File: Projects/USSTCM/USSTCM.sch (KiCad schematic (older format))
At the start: 26 parts, among them IC1 REG1117, IC2 REG1117, Q1 DMG1012T, Q2 DMG1012T, U1 RASPI

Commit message: sync for working with liz
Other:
- moved on the sheet: ACT55, C1, C10, C15, C17, C18, C19, C2, C20, C46, C6, C8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

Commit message: Refactoring Compute Module project for 2017 USST KiCad library format
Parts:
- ACT55, PWR1: symbol LED_LEDCHIP-LED0603 -> LED
- C1, C10, C17, C18, C19, C2, C20, C46, C9: symbol RCL_C-EUC0805 -> C
- C15: symbol RCL_C-EUC0603 -> C
- C6, C8: symbol RCL_CPOL-EU153CLV-0605 -> CP
- IC1, IC2: symbol BURR-BROWN_REG1117 -> REG1117
- Q1, Q2: symbol TRANSISTOR-FET_BSA223SP -> Q_PMOS_GDS
- R1, R2, R21, R3, R35, R4, R5: symbol RCL_R-EU_R0603 -> R
- U1: symbol RASPI_RASPI -> RASPI_CM
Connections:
- net 1V8: now also C6.1, R2.1; no longer C6.+, R2.2
- net 3V3: now also C8.1, R21.1, R35.1; no longer C8.+, R21.2, R35.2
- net GND: now also C6.2, C8.2, PWR1.1 (K), Q2.2 (D), R1.2, R3.1, R4.1, R5.1; no longer C6.-, C8.-, PWR1.C, Q2.3 (S), R1.1, R3.2, R4.2, R5.2
- net GPIO28: now also R4.2; no longer R4.1
- net GPIO29: now also R3.2; no longer R3.1
- net GPIO44: now also R5.2; no longer R5.1
- net VUSB_BOOT: now also R1.1; no longer R1.2
- removed net N$1: PWR1.A, R21.1
- net N$3: no longer names the net of Q1.2 (D)
- net N$3: now also ACT55.1 (K), Q2.3 (S); no longer U1.2 (EMMC_DISABLE_N)
- removed net N$4: ACT55.A, R35.1
- removed net N$5: ACT55.C, Q1.3 (S), Q2.2 (D)
- net N$6: no longer names the net of Q2.1 (G), U1.90 (GPIO47_1V8)
- net N$6: now also R2.2; no longer R2.1
- new net: ACT55.2 (A), R35.2
- new net: Q1.3 (S), U1.2 (EMMC_DISABLE_N)
- new net: PWR1.2 (A), R21.2
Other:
- moved on the sheet: IC1, IC2, U1

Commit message: More organization of CMIO board
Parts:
- removed C1, C17, C18, C19, C2, C20, C46: 10u, USSTCM:RCL_C0805, symbol C
- removed C6, C8: ~, USSTCM:RCL_153CLV-0605, symbol CP
- removed IC1, IC2: REG1117, USSTCM:BURR-BROWN_SOT223, symbol REG1117
- removed PWR1: ~, USSTCM:LED_CHIP-LED0603, symbol LED
- removed R21: 1k8, USSTCM:RCL_R0603, symbol R
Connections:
- net 1V8 renamed +1V8
- net 3V3 renamed +3V3
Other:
- note added: "DAC 2v5 is Unused"
- note added: "NOTE: Default Device Tree Source\nhttps://github.com/raspberrypi/firmware/blob/master/extra/dt-blob.dts"
- note added: "This block works with the USB interface to diable the EMMC for flashing"

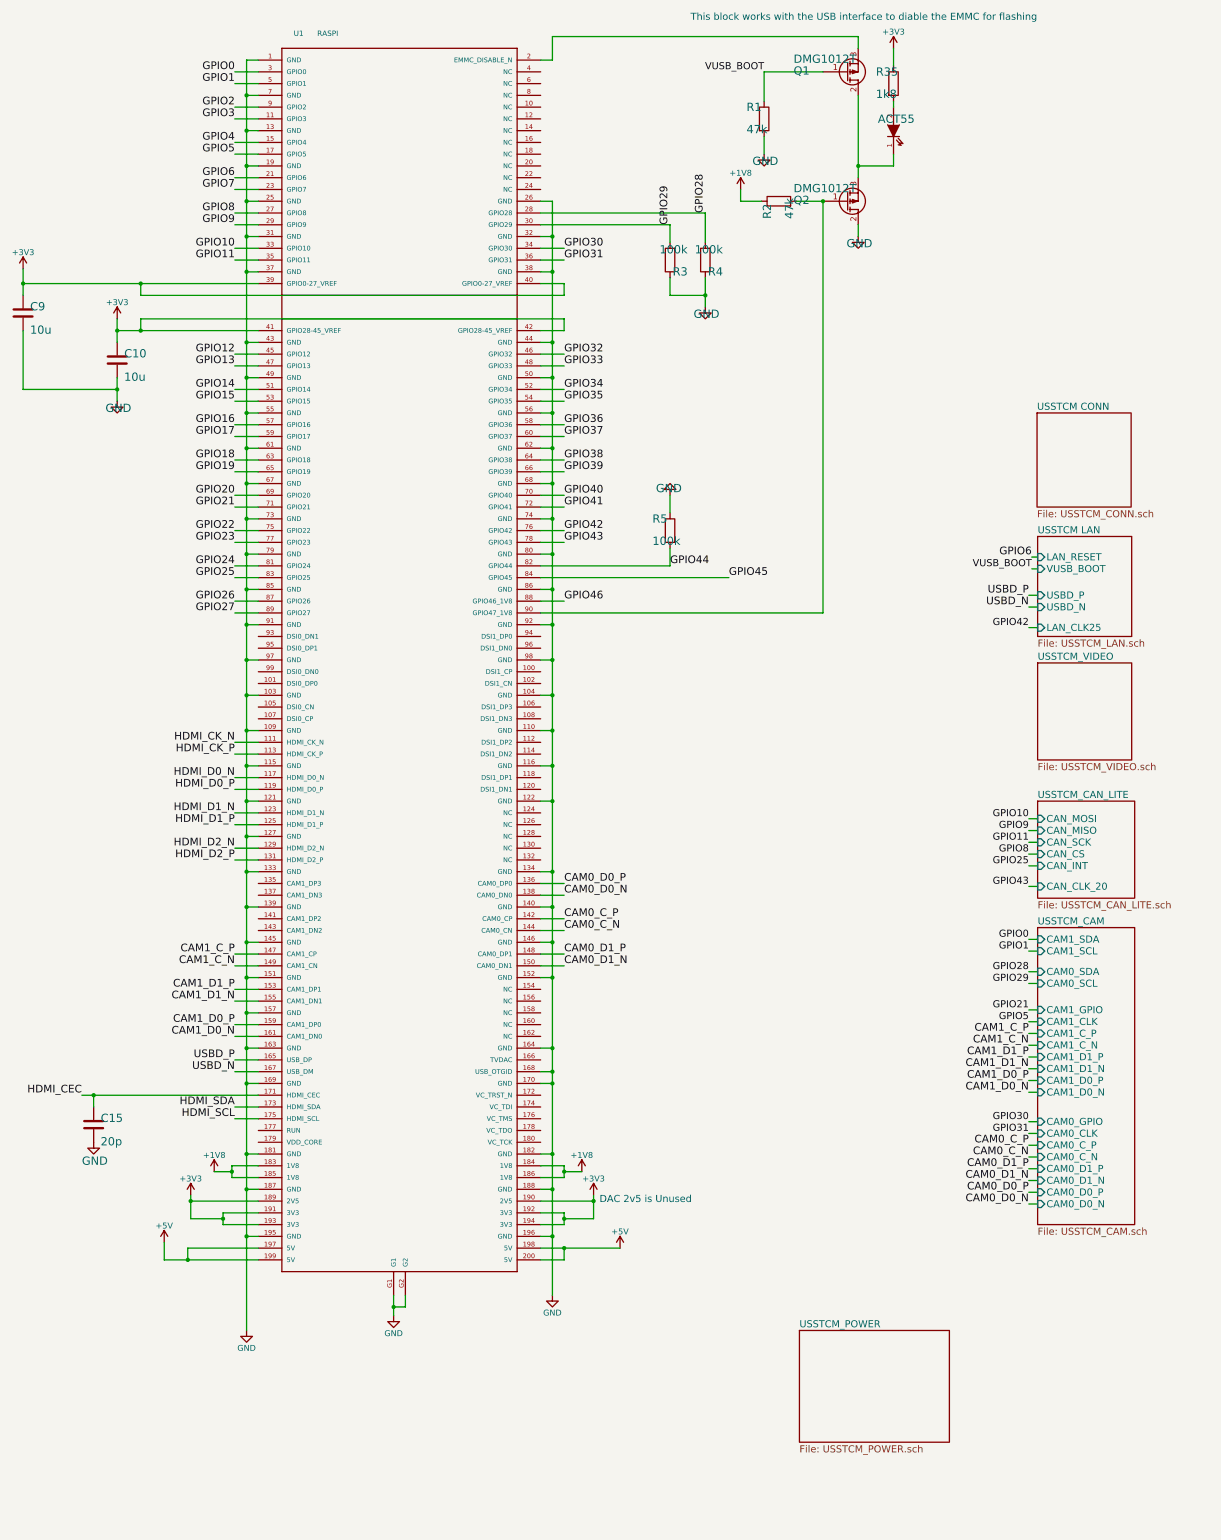
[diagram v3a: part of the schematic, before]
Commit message: added differential routes
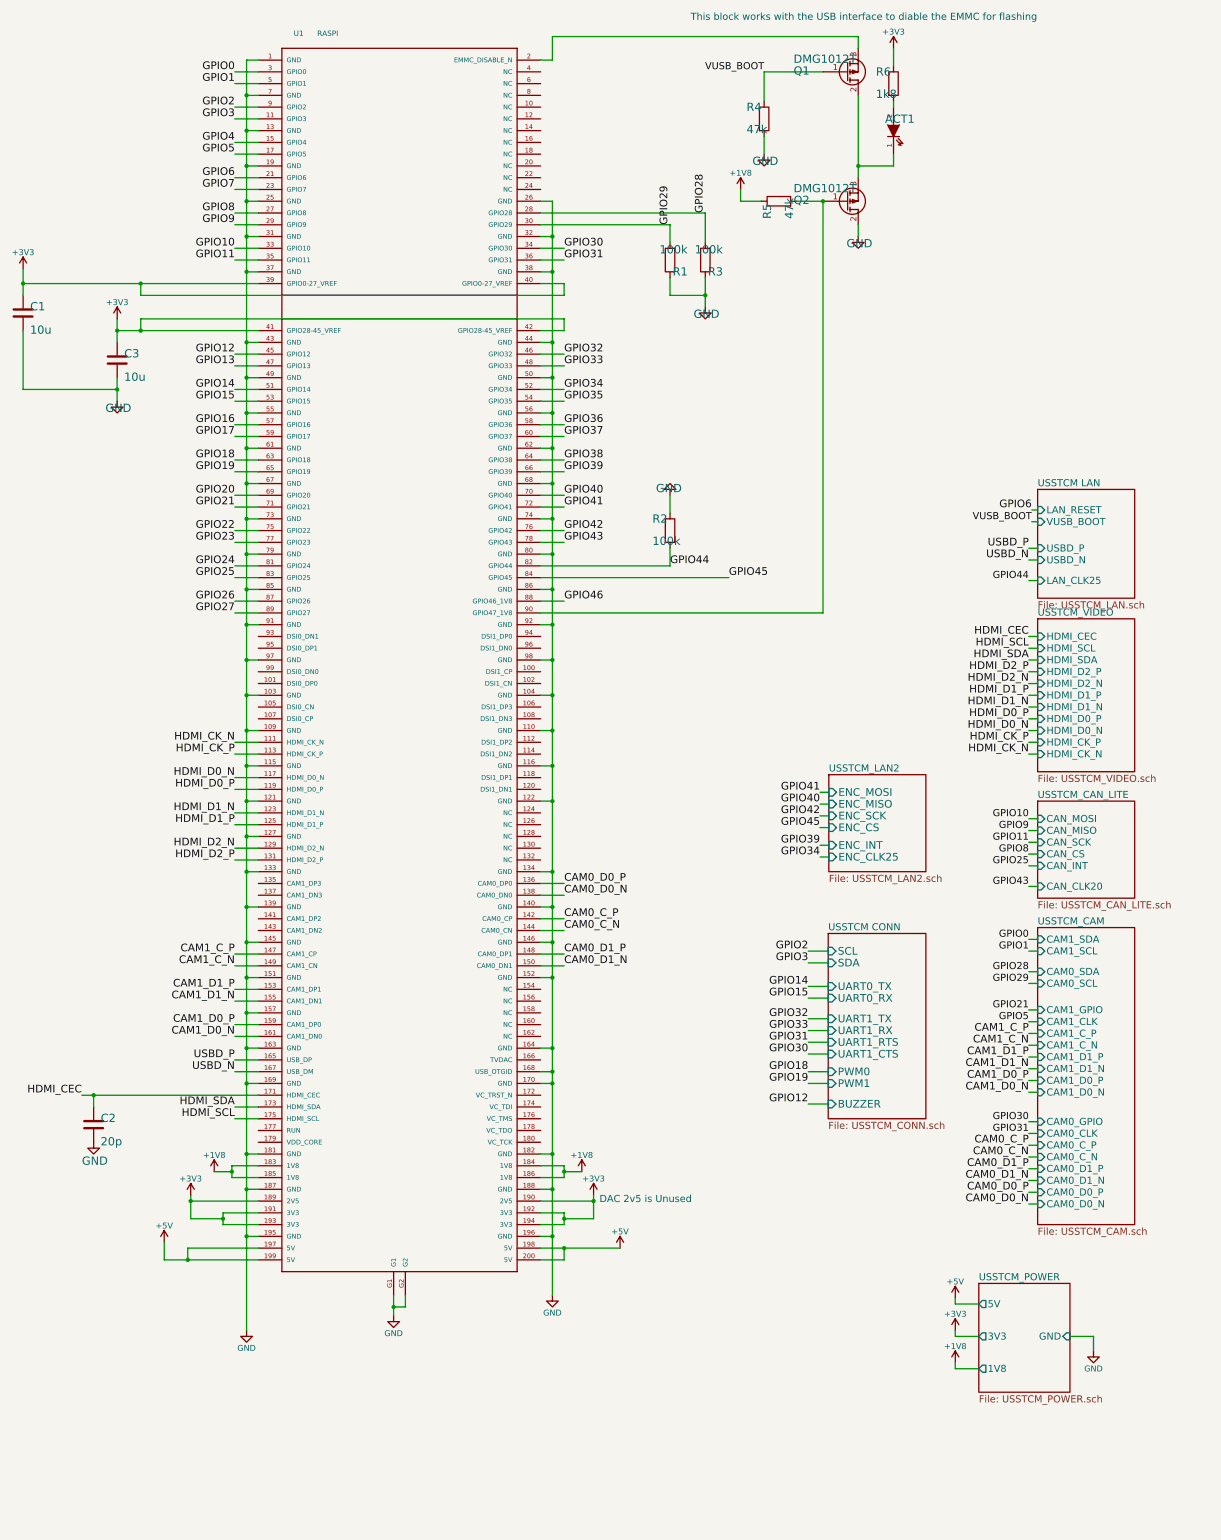
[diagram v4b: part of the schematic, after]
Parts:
- ACT1: renamed from ACT55; footprint USSTCM:LED_CHIP-LED0603 -> LEDs:LED_0805
- C1: renamed from C9; footprint USSTCM:RCL_C0805 -> Capacitors_SMD:C_0805
- C2: renamed from C15; footprint USSTCM:RCL_C0603 -> Capacitors_SMD:C_0805
- C3: renamed from C10; footprint USSTCM:RCL_C0805 -> Capacitors_SMD:C_0805
- R1: renamed from R3; footprint USSTCM:RCL_R0603 -> Resistors_SMD:R_0805
- R2: renamed from R5; footprint USSTCM:RCL_R0603 -> Resistors_SMD:R_0805
- R3: renamed from R4; footprint USSTCM:RCL_R0603 -> Resistors_SMD:R_0805
- R4: renamed from R1; footprint USSTCM:RCL_R0603 -> Resistors_SMD:R_0805
- R5: renamed from R2; footprint USSTCM:RCL_R0603 -> Resistors_SMD:R_0805
- R6: renamed from R35; footprint USSTCM:RCL_R0603 -> Resistors_SMD:R_0805
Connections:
- wire segments 235 -> 271
